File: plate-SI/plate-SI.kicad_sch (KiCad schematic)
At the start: 10 parts, among them J1 Conn_01x07, J2 Conn_01x04

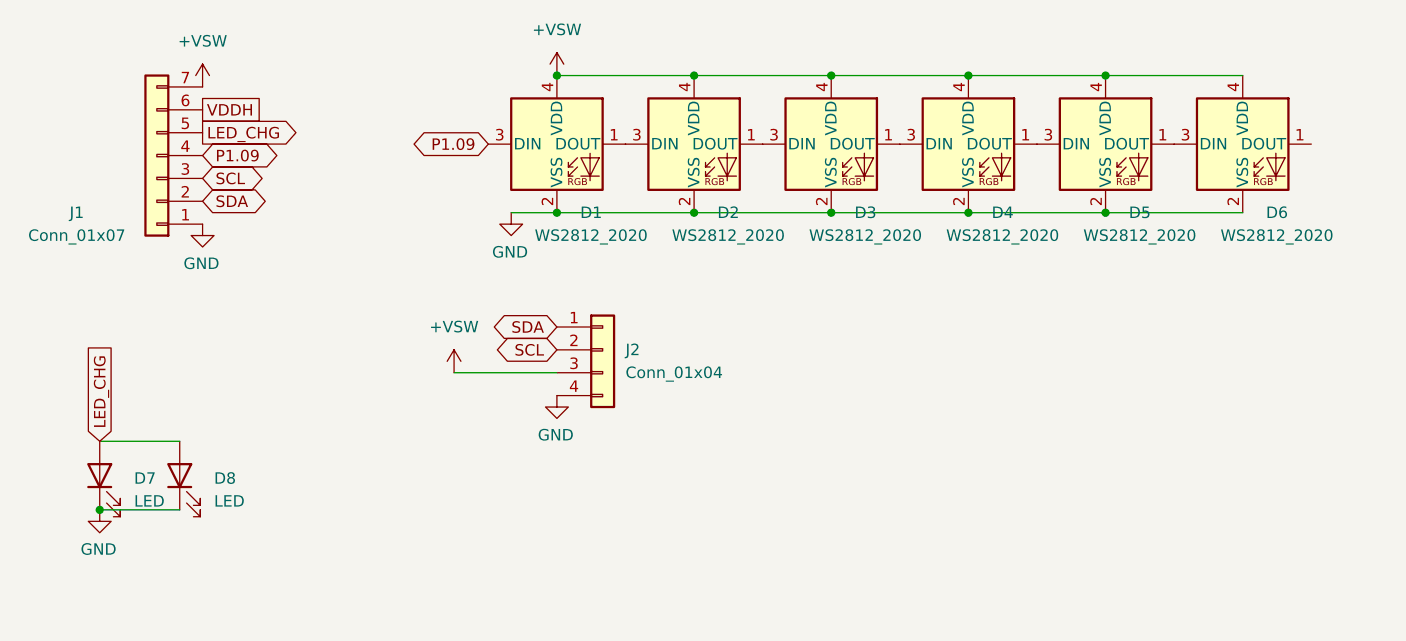
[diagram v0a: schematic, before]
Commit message: fixed SI plate, added MX plate
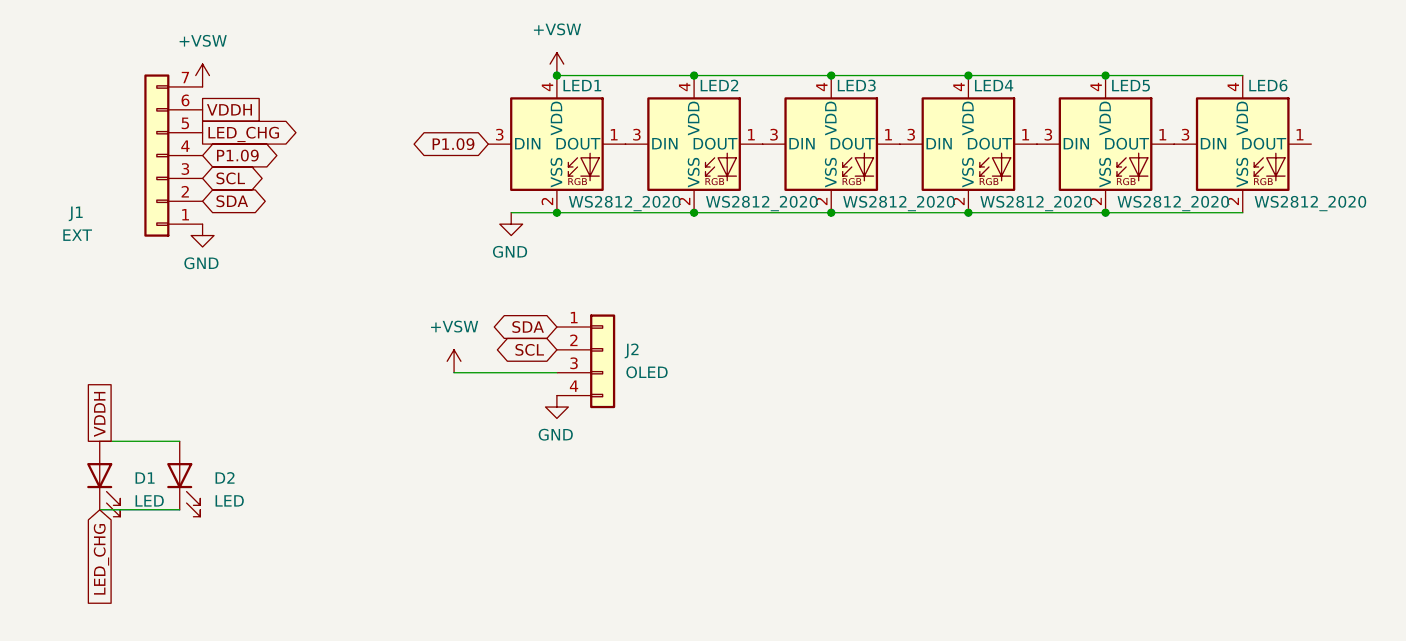
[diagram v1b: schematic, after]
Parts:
- J1: value Conn_01x07 -> EXT
- J2: value Conn_01x04 -> OLED
- LED1: renamed from D1; footprint marbastlib-various:LED_WS2812_2020 -> PCM_marbastlib-various:LED_WS2812_2020; symbol marbastlib-various:WS2812_2020 -> PCM_marbastlib-various:WS2812_2020
- LED2: renamed from D2; footprint marbastlib-various:LED_WS2812_2020 -> PCM_marbastlib-various:LED_WS2812_2020; symbol marbastlib-various:WS2812_2020 -> PCM_marbastlib-various:WS2812_2020
- LED3: renamed from D3; footprint marbastlib-various:LED_WS2812_2020 -> PCM_marbastlib-various:LED_WS2812_2020; symbol marbastlib-various:WS2812_2020 -> PCM_marbastlib-various:WS2812_2020
- LED4: renamed from D4; footprint marbastlib-various:LED_WS2812_2020 -> PCM_marbastlib-various:LED_WS2812_2020; symbol marbastlib-various:WS2812_2020 -> PCM_marbastlib-various:WS2812_2020
- LED5: renamed from D5; footprint marbastlib-various:LED_WS2812_2020 -> PCM_marbastlib-various:LED_WS2812_2020; symbol marbastlib-various:WS2812_2020 -> PCM_marbastlib-various:WS2812_2020
- LED6: renamed from D6; footprint marbastlib-various:LED_WS2812_2020 -> PCM_marbastlib-various:LED_WS2812_2020; symbol marbastlib-various:WS2812_2020 -> PCM_marbastlib-various:WS2812_2020
- renumbered D7 to D1, D8 to D2
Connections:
- net GND: no longer D1.1 (K), D2.1 (K)
- net LED_CHG: now also D1.1 (K), D2.1 (K); no longer D1.2 (A), D2.2 (A)
- net VDDH: now also D1.2 (A), D2.2 (A)
